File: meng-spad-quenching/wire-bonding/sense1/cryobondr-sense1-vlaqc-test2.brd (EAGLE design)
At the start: 46 x 46 mm, 43 parts, among them IC1 SENSE1, U1 SN74LVC1G34DBVT, U2 SN74LVC1G34DBVT, X1 HTR2, X10 R3_OUT, X11 R4_OUT, X12 R4_IBIAS, X2 R4_VA, X3 R3_VA, X4 HTR1, X5 SPAD2, X6 R3_IBIAS, X7 R3_2V5, X8 R4_2V5, X9 SPAD1

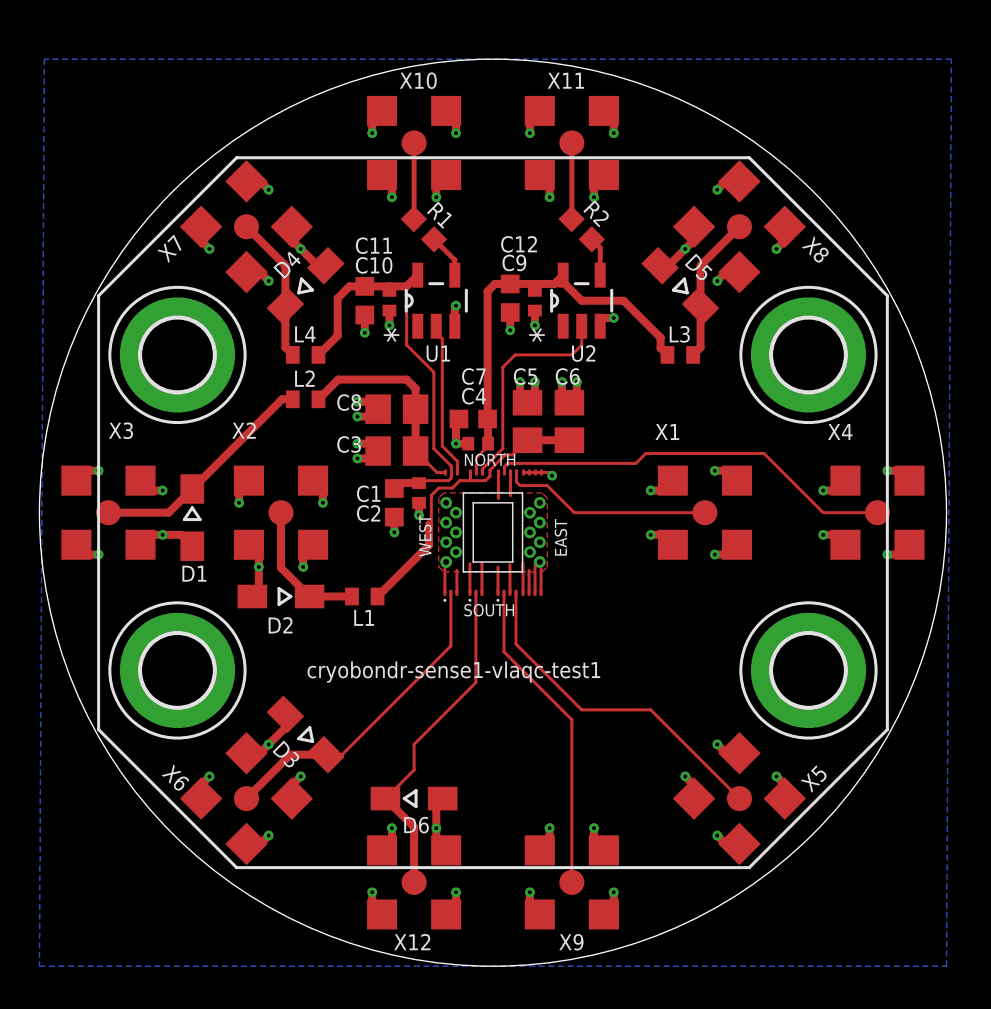
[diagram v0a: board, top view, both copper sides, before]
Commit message: Made new cryo testing board for sense1 AQC rev. 5
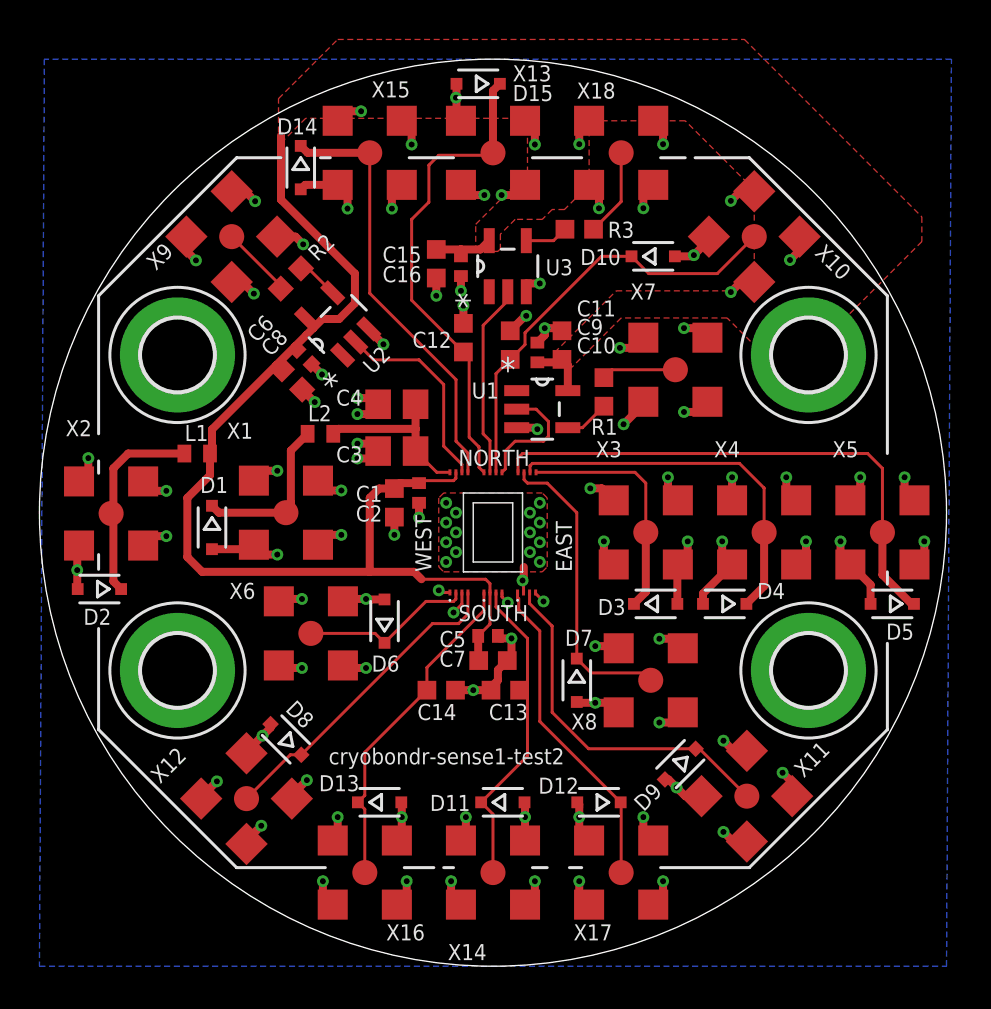
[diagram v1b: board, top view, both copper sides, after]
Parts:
- removed L3, L4: Samsung CIM05J152NC, meng:R0402
- added C13, C14: CAP CER 0.1UF 0603 16V, rcl-modified-footprints:C0603
- added C15: IPDiA 935131424510, rcl-modified-footprints:C0402
- added C16: IPDiA 935131425610, rcl-modified-footprints:C0603
- added D10, D11, D12, D13, D15, D7, D9: DF2B29FU,H3F, diode:SOD323-R
- added D14, D8: UCLAMP3301D.TCT, diode:SOD323-R
- added R3: Vishay FC0603E50R0BTBST1, rcl-modified-footprints:R0603
- added U3: SN74LVC1G34DBVT, Texas Instruments_By_element14_Batch_1:SOT95P280X145-5N
- added X13: PS2_B2, meng:MMCX-SMT-BIGPADS
- added X14: PS2_B1, meng:MMCX-SMT-BIGPADS
- added X15: R5_BUP, meng:MMCX-SMT-BIGPADS
- added X16: PS1_B1, meng:MMCX-SMT-BIGPADS
- added X17: SPAD1, meng:MMCX-SMT-BIGPADS
- added X18: P1_OUT, meng:MMCX-SMT-BIGPADS
- C10: value IPDiA 935131424510 -> CAP CER 0.1UF 0603 16V; device rcl-modified-footprints:C0402 -> rcl-modified-footprints:C0603
- C12: value IPDiA 935131425610 -> CAP CER 0.1UF 0603 16V
- C4: value IPDiA 935131424510 -> ECH-U1C103JB5; device rcl-modified-footprints:C0402 -> rcl-modified-footprints:C0805
- C5: value ECP-U1C104MA5 -> IPDiA 935131424510; device rcl-modified-footprints:C0805 -> rcl-modified-footprints:C0402
- C6: value ECH-U1C103JB5 -> IPDiA 935131425610; device rcl-modified-footprints:C0805 -> rcl-modified-footprints:C0603
- C8: value ECH-U1C103JB5 -> IPDiA 935131424510; device rcl-modified-footprints:C0805 -> rcl-modified-footprints:C0402
- D1: value DF2B36FU,H3F -> DF2B29FU,H3F; device diode:SOD323-W -> diode:SOD323-R
- D2: value DF2B36FU,H3F -> UCLAMP3301D.TCT; device diode:SOD323-W -> diode:SOD323-R
- D3, D4, D5: value UCLAMP3301D.TCT -> DF2B29FU,H3F; device diode:SOD323-W -> diode:SOD323-R
- D6: device diode:SOD323-W -> diode:SOD323-R
- IC1: device meng:SENSE1-WIREBOND-VLAQC-TEST1 -> meng:SENSE1-WIREBOND-VLAQC-TEST2
- X1: value HTR2 -> R5_VA
- X10: value R3_OUT -> PS1_B2
- X11: value R4_OUT -> SPAD2
- X12: value R4_IBIAS -> R5_BDN
- X2: value R4_VA -> VDD2V5
- X3: value R3_VA -> S2_HTR1
- X4: value HTR1 -> S2_HTR2
- X5: value SPAD2 -> S1_HTR2
- X6: value R3_IBIAS -> R5_HOLDOFF
- X7: value R3_2V5 -> P2_OUT
- X8: value R4_2V5 -> S1_HTR1
- X9: value SPAD1 -> R5_OUT
- moved X9 37.0 mm to (-13.2, 14.0), turned to 45 degrees
- moved X11 34.3 mm to (12.9, -14.4), turned to 45 degrees
- moved X3 27.3 mm to (7.75, -1.00)
- moved D4 26.7 mm to (11.8, -4.62), turned to 180 degrees
- moved X8 23.4 mm to (8.00, -8.50), turned to 0 degrees
- moved X7 22.9 mm to (9.25, 7.25), turned to 0 degrees
- moved X1 21.2 mm to (-10.5, 0.00)
- moved D5 19.4 mm to (20.2, -4.62), turned to 180 degrees
- moved D3 18.9 mm to (8.25, -4.62), turned to 0 degrees
- moved X10 17.9 mm to (13.2, 14.0), turned to 45 degrees
- moved X5 15.3 mm to (19.8, -1.00), turned to 0 degrees
- moved R2 15.0 mm to (-10.2, 11.9), turned to 225 degrees
- moved C6 14.2 mm to (-10.2, 6.76), turned to 315 degrees
- moved U2 12.4 mm to (-7.88, 9.57), turned to 135 degrees
- moved R1 12.3 mm to (5.62, 6.12), turned to 90 degrees
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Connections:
- net R3_Y renamed P2_Y
- net R4_Y renamed R5_Y
- removed net AQCR3_IBIAS: D3.C, IC1.AQCR3_HOLDOFF_IBIAS, X6.S
- removed net AQCR3_VA: D1.C, L2.2, X3.S
- removed net AQCR3_VA_FILT: C3.1, C8.1, IC1.AQCR3_SPAD_CATHODE, L2.1
- removed net AQCR3_VDD: D4.C, L4.1, X7.S
- removed net AQCR3_VDD_FILT: C1.1, C10.1, C11.1, C2.1, IC1.AQCR3_VDD2V5, L4.2, U1.5
- removed net AQCR4_AV_DET: IC1.AQCR4_AV_DET, U2.2
- removed net AQCR4_IBIAS: D6.C, IC1.AQCR4_HOLDOFF_IBIAS, X12.S
- removed net AQCR4_VA: D2.C, L1.2, X2.S
- removed net AQCR4_VA_FILT: C5.1, C6.1, IC1.AQCR4_SPAD_CATHODE, L1.1
- removed net AQCR4_VDD: D5.C, L3.1, X8.S
- removed net AQCR4_VDD_FILT: C12.1, C4.1, C7.1, C9.1, IC1.AQCR4_VDD2V5, L3.2, U2.5
- removed net R3_Y_R: R1.2, X10.S
- removed net R4_Y_R: R2.2, X11.S
- new net AQCR5_VA_CONN: D1.C, L2.2, X1.S
- new net AQCR5_VA_FILT: C3.1, C4.1, IC1.AQCR5_SPAD_CATHODE, L2.1
- new net P1_Y: R3.1, U3.4
- new net P1_Y_R: R3.2, X18.S
- new net P2_Y_R: R1.2, X7.S
- new net PQC1_AV_DET: IC1.PQC_SPAD1_AV_DET, U3.2
- new net PQC2_AV_DET: IC1.PQC_SPAD2_AV_DET, U1.2
- new net PQC_SPAD1_BIAS1: C14.1, D13.C, IC1.PQC_SPAD1_BIAS1, X16.S
- new net PQC_SPAD1_BIAS2: C12.1, D15.C, IC1.PQC_SPAD1_BIAS2, X13.S
- new net PQC_SPAD2_BIAS1: C13.1, D11.C, IC1.PQC_SPAD2_BIAS1, X14.S
- new net PQC_SPAD2_BIAS2: C10.1, D10.C, IC1.PQC_SPAD2_BIAS2, X10.S
- new net R5_BIAS_DOWN: D8.C, IC1.AQCR5_BIAS_DOWN, X12.S
- new net R5_BIAS_UP: D14.C, IC1.AQCR5_BIAS_UP, X15.S
- new net R5_HOLDOFF: D6.C, IC1.AQCR5_HOLDOFF_VBIAS_PAD, X6.S
- new net R5_Y_R: R2.2, X9.S
- new net SPAD1_HTR1: D3.C, IC1.SG_SPAD2_HEATER2, X3.S
- new net SPAD2_HTR1: D4.C, IC1.SG_SPAD2_HEATER1, X4.S
- new net VDD2V5_CONN: D2.C, L1.1, X2.S
- new net VDD2V5_FILT: C1.1, C11.1, C15.1, C16.1, C2.1, C5.1, C6.1, C7.1, C8.1, C9.1, IC1.AQCR5_VDD2V5, IC1.PQC_VDD2V5, L1.2, U1.5, U2.5, U3.5
- net AQCR3_AV_DET: now also IC1.AQCR5_AV_DET, U2.2; no longer IC1.AQCR3_AV_DET, U1.2
- net GND: now also C13.2, C14.2, C15.2, C16.2, D10.A, D11.A, D12.A, D13.A, D14.A, D15.A, D7.A, D8.A, D9.A, IC1.AQCR5_GND1, IC1.AQCR5_GND2, IC1.PQC_GND, IC1.SG_SPAD1_ANODE, IC1.SG_SPAD2_ANODE, U3.3, X13.G1, X13.G2, X13.G3, X13.G4, X14.G1, X14.G2, X14.G3, X14.G4, X15.G1, X15.G2, X15.G3, X15.G4, X16.G1, X16.G2, X16.G3, X16.G4, X17.G1, X17.G2, X17.G3, X17.G4, X18.G1, X18.G2, X18.G3, X18.G4; no longer IC1.AQCR3_GND, IC1.AQCR3_GUARD_RING, IC1.AQCR4_GND, IC1.AQCR4_GUARD_RING, IC1.SPAD1_ANODE, IC1.SPAD1_HEATER1, IC1.SPAD2_ANODE, IC1.SPAD2_HEATER1, IC1.SPAD3_ANODE, IC1.SPAD3_CATHODE, IC1.SPAD3_HEATER1, IC1.SPAD3_HEATER2, IC1.SPAD4_ANODE, IC1.SPAD4_CATHODE, IC1.SPAD4_HEATER1, IC1.SPAD4_HEATER2
- net SPAD1_CATH: now also D12.C, IC1.SG_SPAD1_CATHODE, X17.S; no longer IC1.SPAD1_CATHODE, X9.S
- net SPAD1_HTR: now also D7.C, IC1.SG_SPAD1_HEATER2, X8.S; no longer IC1.SPAD1_HEATER2, X4.S
- net SPAD2_CATH: now also D9.C, IC1.SG_SPAD2_CATHODE, X11.S; no longer IC1.SPAD2_CATHODE, X5.S
- net SPAD2_HTR: now also D5.C, IC1.SG_SPAD1_HEATER1, X5.S; no longer IC1.SPAD2_HEATER2, X1.S
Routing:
- net VDD2V5_FILT: track 0.00 -> 63.3 mm
- net GND: track 109.9 -> 147.6 mm, vias 80 -> 109
- net PQC_SPAD1_BIAS2: track 0.00 -> 24.6 mm
- net PQC_SPAD2_BIAS2: track 0.00 -> 22.1 mm
- net R5_BIAS_UP: track 0.00 -> 21.9 mm
- net AQCR3_VDD_FILT: track 21.8 -> 0.00 mm
- net AQCR4_VDD_FILT: track 21.4 -> 0.00 mm
- net SPAD2_HTR1: track 0.00 -> 19.0 mm
- net AQCR4_IBIAS: track 17.2 -> 0.00 mm
- net PQC_SPAD1_BIAS1: track 0.00 -> 17.0 mm
- net SPAD2_HTR: track 10.7 -> 27.2 mm
- net PQC_SPAD2_BIAS1: track 0.00 -> 16.5 mm
- net AQCR3_IBIAS: track 16.3 -> 0.00 mm
- net R5_BIAS_DOWN: track 0.00 -> 16.2 mm
- net AQCR4_VA_FILT: track 15.3 -> 0.00 mm
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- added copper zone on layer 1, net VDD2V5_FILT
- removed copper zone on layer 1, net AQCR4_VA_FILT
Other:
- board text added: "cryobondr-sense1-test2"
- board text removed: "cryobondr-sense1-vlaqc-test1"
